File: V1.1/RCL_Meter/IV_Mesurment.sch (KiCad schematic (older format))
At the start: 6 parts

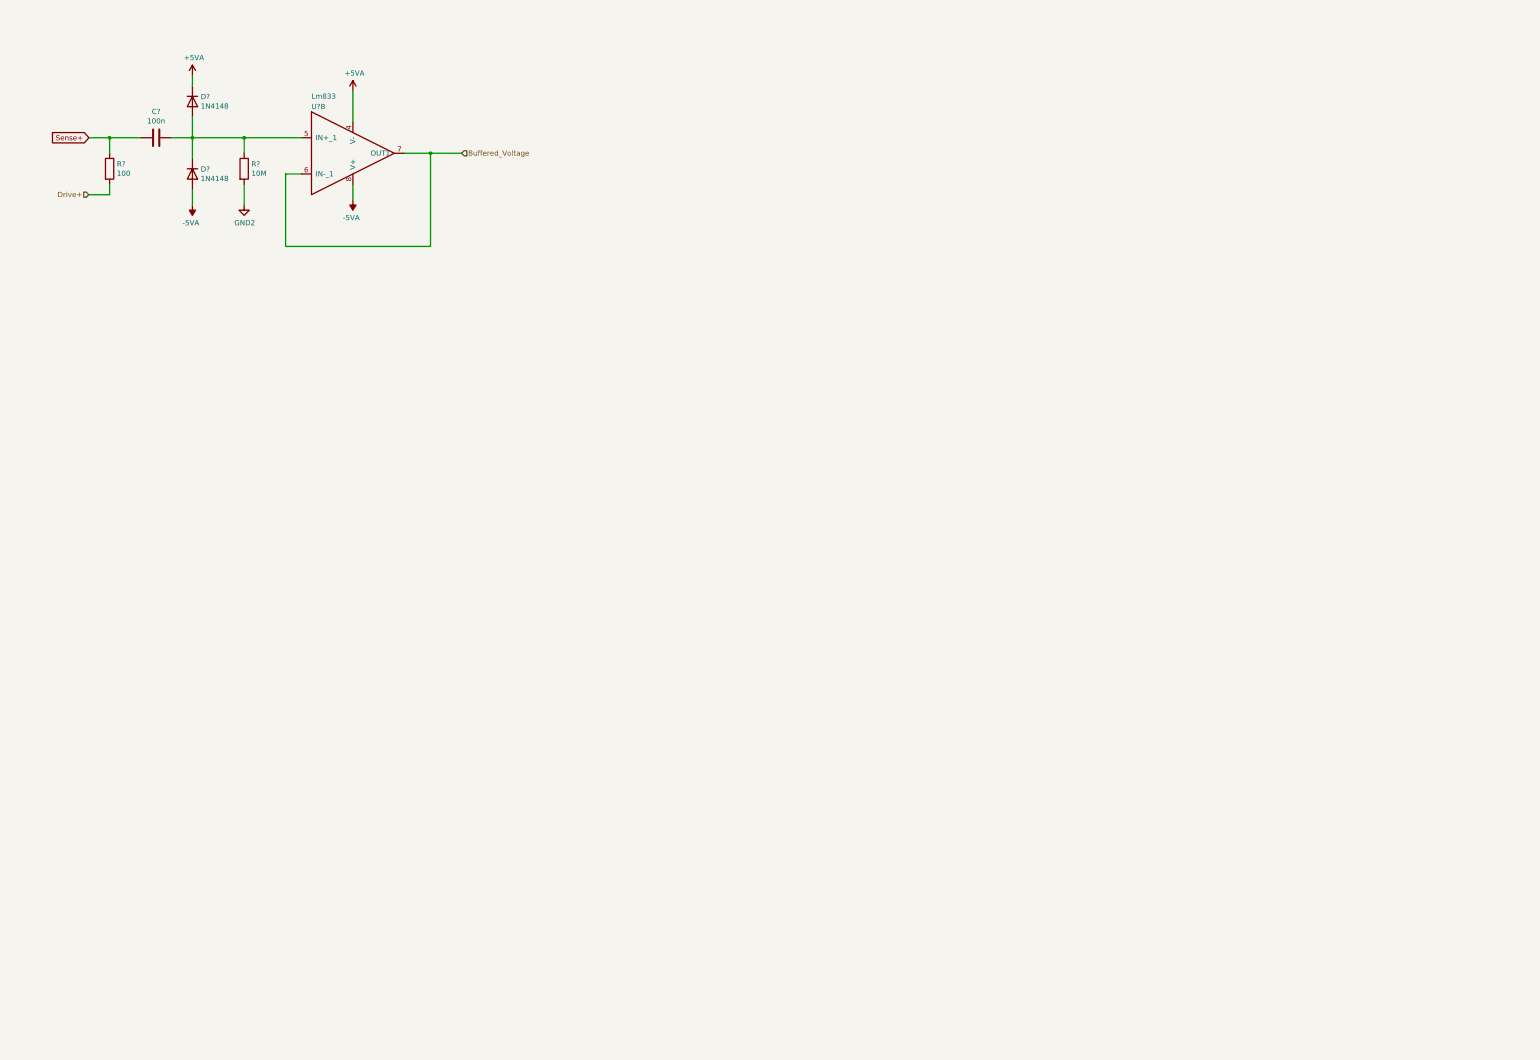
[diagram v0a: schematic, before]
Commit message: added a PGA amplifier to instrumentation amplifier output
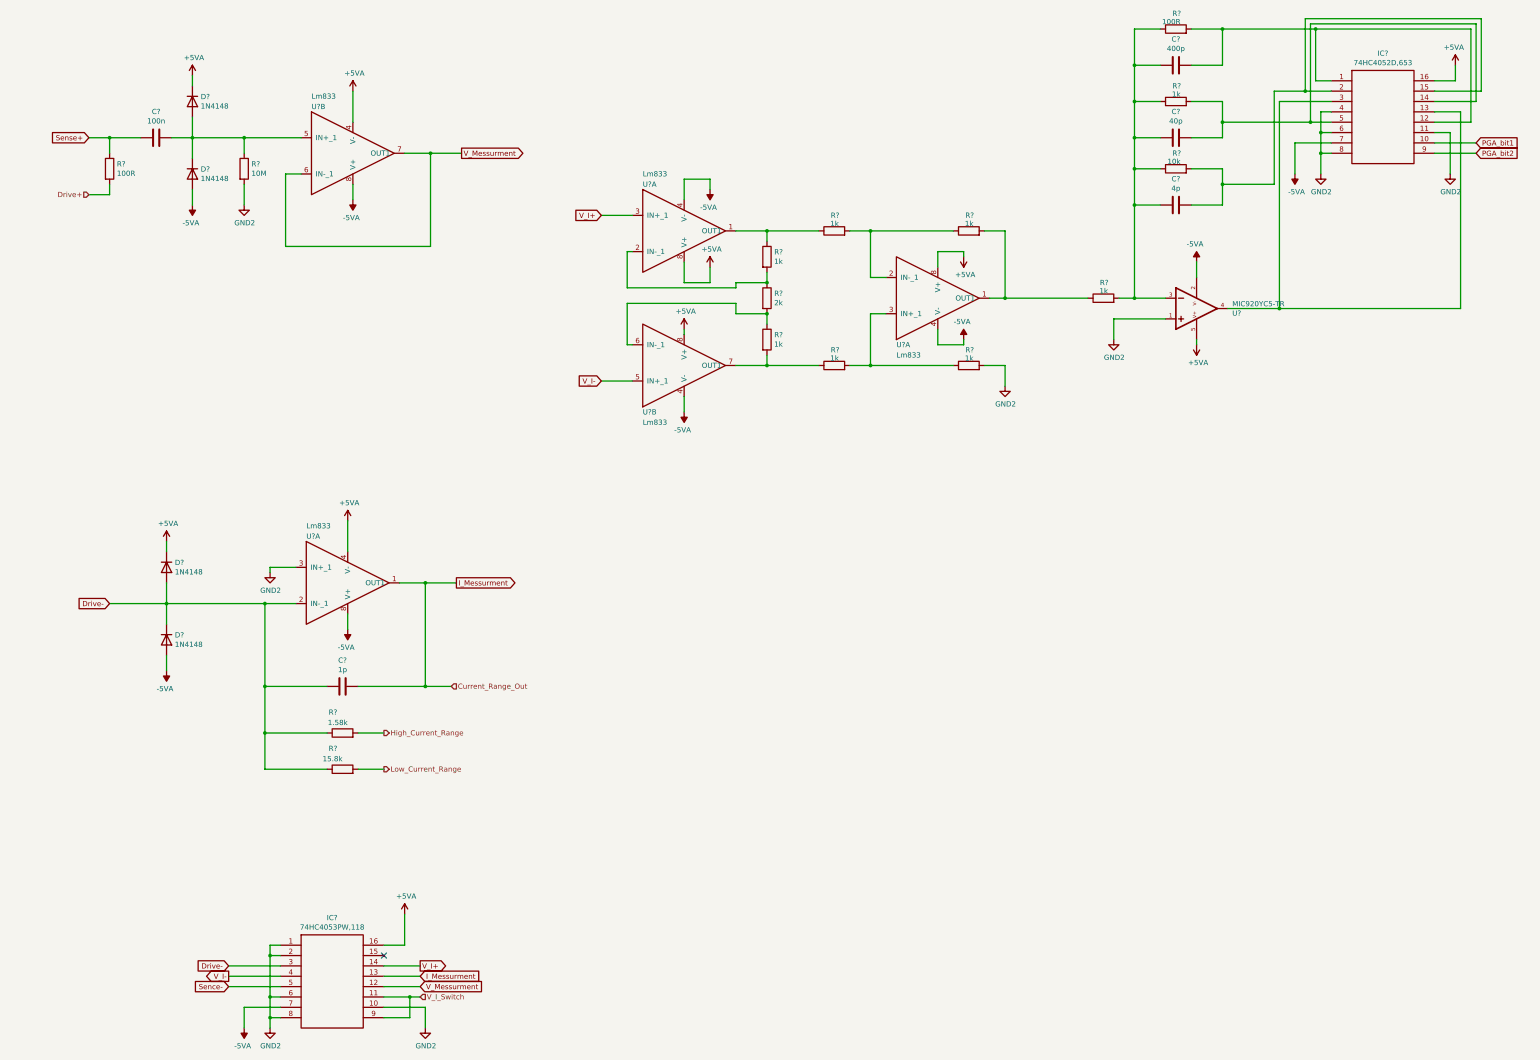
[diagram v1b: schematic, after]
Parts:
- added C?: 1p, symbol Device:C
- added C?: 400p, symbol Device:C
- added C?: 40p, symbol Device:C
- added C?: 4p, symbol Device:C
- added D? (x2): 1N4148, Diode_THT:D_DO-35_SOD27_P7.62mm_Horizontal, symbol Diode:1N4148
- added IC?: 74HC4053PW,118, SOP65P640X110-16N, symbol 74HC4053PW_118:74HC4053PW,118
- added IC?: 74HC4052D,653, SOIC127P600X175-16N, symbol 74HC4052D_653:74HC4052D,653
- added R?: 1.58k, symbol Device:R
- added R?: 15.8k, symbol Device:R
- added R? (x8): 1k, symbol Device:R
- added R?: 10k, symbol Device:R
- added R?: 100R, symbol Device:R
- added R?: 2k, symbol Device:R
- added U? (x4): Lm833, symbol Amplifier_Operational2:Lm833
- added U?: MIC920YC5-TR, SOT65P210X110-5N, symbol MIC920YC5-TR:MIC920YC5-TR
- R?: value 100 -> 100R
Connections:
- net +5VA: now also D?.1 (K), IC?.16, IC?.16, U?.4 (V-), U?.5, U?.8 (V+), U?.8 (V+), U?.8 (V+)
- net -5VA: now also D?.2 (A), IC?.7, IC?.7, U?.2, U?.4 (V-), U?.4 (V-), U?.4 (V-), U?.8 (V+)
- net GND2: now also IC?.1, IC?.10, IC?.11, IC?.2, IC?.4, IC?.6, IC?.6, IC?.8, IC?.8, R?.2, U?.1, U?.3 (IN+_1)
- net Buffered_Voltage renamed V_Messurment
- net V_Messurment: now also IC?.12
- new net: C?.2, C?.2, C?.2, R?.1, R?.1, R?.1, R?.2, U?.3
- new net: IC?.13, IC?.3, U?.4
- new net: C?.1, IC?.14, IC?.5, R?.2
- new net: C?.1, IC?.15, IC?.2, R?.2
- new net: C?.1, IC?.1, IC?.12, R?.2
- new net: R?.1, R?.1, U?.1 (OUT1)
- new net: R?.1, R?.2, U?.2 (IN-_1) (x2)
- new net: R?.1, R?.2, U?.6 (IN-_1)
- new net: R?.1, R?.2, U?.7 (OUT1)
- new net: R?.1, R?.2, U?.1 (OUT1)
- new net: R?.1, R?.2, U?.3 (IN+_1)
- new net Drive-: C?.2, D?.1 (K), D?.2 (A), IC?.3, R?.1, R?.1, U?.2 (IN-_1)
- new net High_Current_Range: R?.2
- new net I_Messurment: C?.1, IC?.13, U?.1 (OUT1)
- new net Low_Current_Range: R?.2
- new net PGA_bit1: IC?.10
- new net PGA_bit2: IC?.9
- new net Sence-: IC?.5
- new net V_I+: IC?.14, U?.3 (IN+_1)
- new net V_I-: IC?.4, U?.5 (IN+_1)
- new net V_I_Switch: IC?.11, IC?.9
- no-connect marks 0 -> 1

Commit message: Created split power supply 12V to +-5V
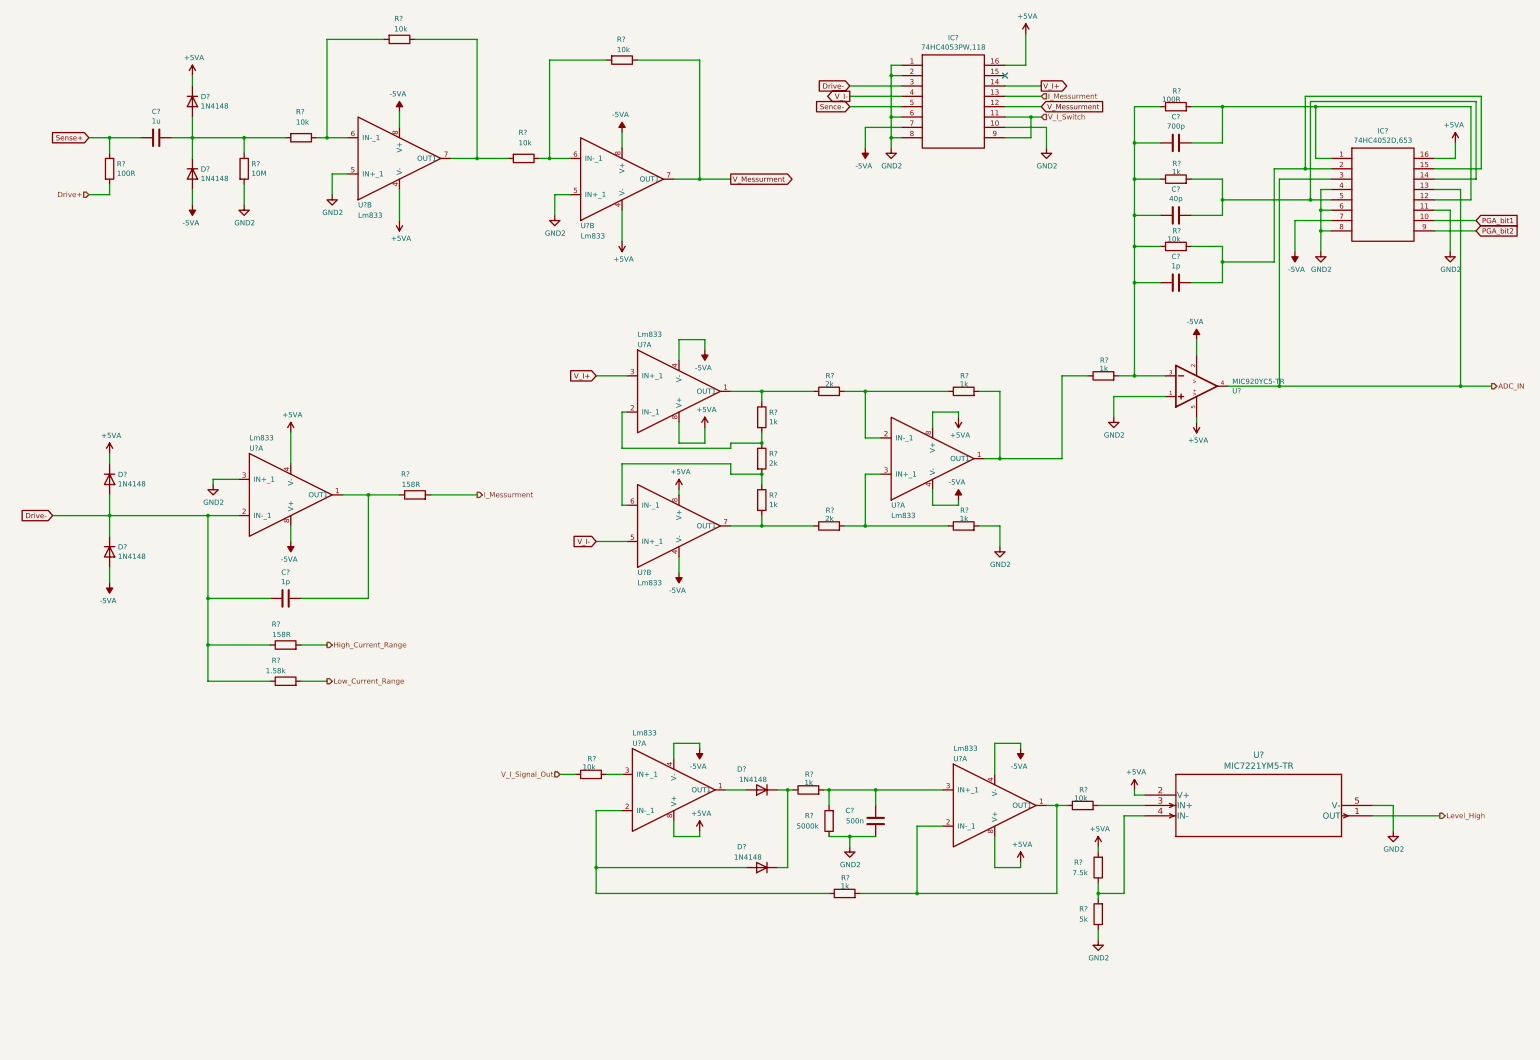
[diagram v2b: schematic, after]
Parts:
- added C?: 500n, symbol Device:C
- added D? (x2): 1N4148, Diode_THT:D_DO-35_SOD27_P7.62mm_Horizontal, symbol Diode:1N4148
- added R? (x6): 10k, symbol Device:R
- added R?: 158R, symbol Device:R
- added R? (x2): 1k, symbol Device:R
- added R?: 5000k, symbol Device:R
- added R?: 7.5k, symbol Device:R
- added R?: 5k, symbol Device:R
- added U? (x3): Lm833, symbol Amplifier_Operational2:Lm833
- added U?: MIC7221YM5-TR, SOT-23-5_M5_MCH, symbol MIC7211:MIC7221YM5-TR
- C?: value 100n -> 1u
- C?: value 400p -> 700p
- C?: value 4p -> 1p
- R?: value 1.58k -> 158R
- R?: value 15.8k -> 1.58k
- R? (x2): value 1k -> 2k
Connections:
- net +5VA: now also R?.2, U?.2 (V+), U?.4 (V-), U?.8 (V+), U?.8 (V+)
- net -5VA: now also U?.4 (V-), U?.4 (V-), U?.8 (V+)
- net GND2: now also U?.5 (IN+_1), C?.2, R?.1, R?.1, U?.5 (IN+_1), U?.5 (V-)
- net I_Messurment: now also R?.2; no longer C?.1, U?.1 (OUT1)
- net V_Messurment: now also R?.1, U?.7 (OUT1); no longer U?.6 (IN-_1), U?.7 (OUT1)
- net at C?.1, D?.1 (K), D?.2 (A)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: now also R?.2; no longer U?.5 (IN+_1)
- net ADC_IN: now reaches IC?.13, IC?.3, U?.4
- new net: R?.1, R?.2, U?.6 (IN-_1) (x2)
- new net: R?.1, R?.2, U?.7 (OUT1)
- new net: C?.1, R?.1, U?.1 (OUT1)
- new net: D?.2 (A), U?.1 (OUT1)
- new net: D?.2 (A), R?.1, U?.2 (IN-_1)
- new net: R?.2, U?.3 (IN+_1)
- new net: R?.1, R?.2, U?.1 (OUT1), U?.2 (IN-_1)
- new net: C?.1, R?.2, R?.2, U?.3 (IN+_1)
- new net: D?.1 (K), D?.1 (K), R?.1
- new net: R?.2, U?.3 (IN+)
- new net: R?.1, R?.2, U?.4 (IN-)
- new net Level_High: U?.1 (OUT)
- new net V_I_Signal_Out: R?.1
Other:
- moved on the sheet: C?, D?, IC?, R?, U?, U?A, U?B
